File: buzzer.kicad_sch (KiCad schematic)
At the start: 4 parts, among them Q801 2N7002

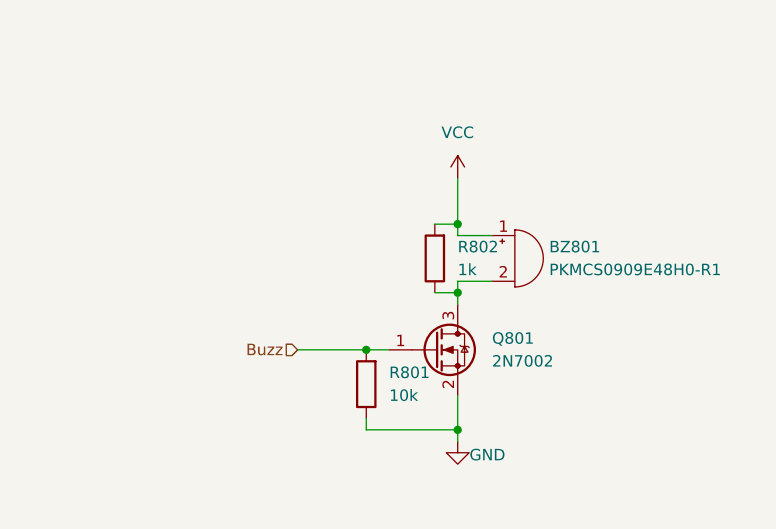
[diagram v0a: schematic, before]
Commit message: Buzzer using high switch
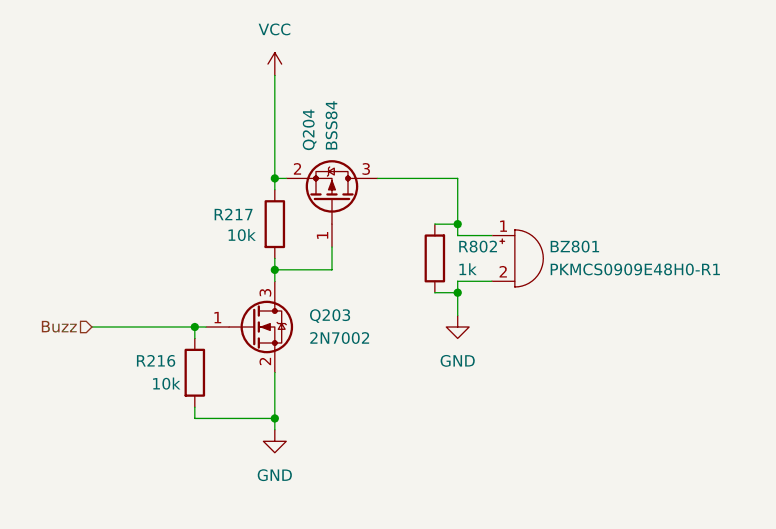
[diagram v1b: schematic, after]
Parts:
- removed Q801: 2N7002, Package_TO_SOT_SMD:SOT-23W_Handsoldering, symbol Transistor_FET:2N7002
- removed R801: 10k, Resistor_SMD:R_1206_3216Metric_Pad1.30x1.75mm_HandSolder, symbol Device:R
- added Q203: 2N7002, Package_TO_SOT_SMD:SOT-23W_Handsoldering, symbol Transistor_FET:2N7002
- added Q204: BSS84, Package_TO_SOT_SMD:SOT-23W_Handsoldering, symbol Transistor_FET:BSS84
- added R216, R217: 10k, Resistor_SMD:R_1206_3216Metric_Pad1.30x1.75mm_HandSolder, symbol Device:R
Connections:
- net Buzz: now also Q203.1 (G), R216.1
- net GND: now also BZ801.2 (-), R802.1, Q203.2 (S), R216.2
- net VCC: now also Q204.2 (S), R217.1; no longer BZ801.1 (+), R802.2
- new net: Q203.3 (D), Q204.1 (G), R217.2
- new net: BZ801.1 (+), Q204.3 (D), R802.2

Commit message: Selected buzzer components
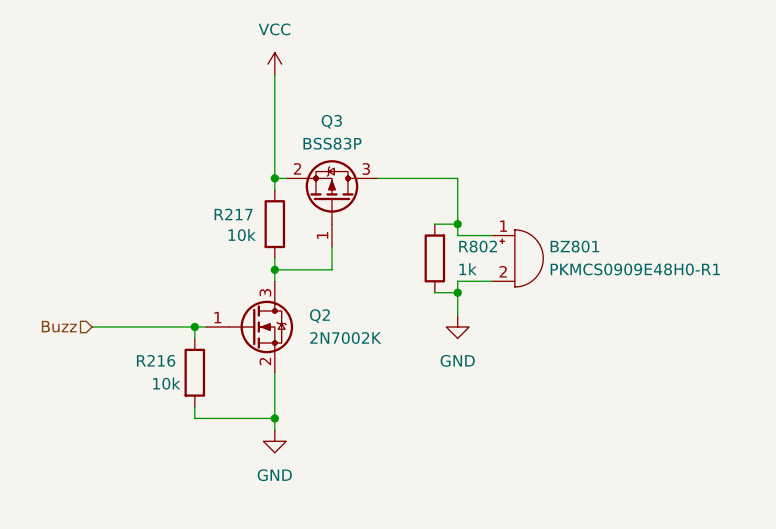
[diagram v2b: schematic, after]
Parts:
- removed Q203: 2N7002, Package_TO_SOT_SMD:SOT-23W_Handsoldering, symbol Transistor_FET:2N7002
- removed Q204: BSS84, Package_TO_SOT_SMD:SOT-23W_Handsoldering, symbol Transistor_FET:BSS84
- added Q2: 2N7002K, Package_TO_SOT_SMD:SOT-23, symbol Transistor_FET:2N7002K
- added Q3: BSS83P, Package_TO_SOT_SMD:SOT-23, symbol Transistor_FET:BSS83P
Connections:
- net Buzz: now also Q2.1 (G)
- net GND: now also Q2.2 (S)
- net VCC: now also Q3.2 (S)
- net at R217.2: now also Q2.3 (D), Q3.1 (G)
- net at BZ801.1 (+), R802.2: now also Q3.3 (D)
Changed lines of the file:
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@@
-	)
-	(symbol
-		(lib_id "Transistor_FET:2N7002")
-		(at 121.92 99.06 0)
-		(unit 1)
-		(exclude_from_sim no)
-		(in_bom yes)
-		(on_board yes)
-		(dnp no)
-		(fields_autoplaced yes)
-		(property "Reference" "Q203"
-			(at 128.27 97.7899 0)
-			(effects
-				(font
-					(size 1.27 1.27)
-				)
-				(justify left)
-			)
-		)
-		(property "Value" "2N7002"
-			(at 128.27 100.3299 0)
-			(effects
-				(font
-					(size 1.27 1.27)
-				)
-				(justify left)
-			)
-		)
-		(property "Footprint" "Package_TO_SOT_SMD:SOT-23W_Handsoldering"
-			(at 127 100.965 0)
-			(effects
-				(font
-					(size 1.27 1.27)
-					(italic yes)
-				)
-				(justify left)
-				(hide yes)
-			)
-		)
-		(property "Datasheet" "https://www.onsemi.com/pub/Collateral/NDS7002A-D.PDF"
-			(at 127 102.87 0)
-			(effects
-				(font
-					(size 1.27 1.27)
-				)
-				(justify left)
-				(hide yes)
-			)
-		)
-		(property "Description" "0.115A Id, 60V Vds, N-Channel MOSFET, SOT-23"
-			(at 121.92 99.06 0)
-			(effects
-				(font
-					(size 1.27 1.27)
-				)
-				(hide yes)
-			)
-		)
-		(pin "3"
-		)
-		(pin "2"
-		)
-		(pin "1"
-		)
-		(instances
-			(project "LifeCounter"
-				(path "/16b3e55a-9d75-49bf-a6fe-25414eb3d7da/ea853267-6be5-4470-9fb8-da1c0cfa6c51"
-					(reference "Q203")
-					(unit 1)
-				)
-			)
-		)
-	)
-	(symbol
-		(lib_id "Transistor_FET:BSS84")
-		(at 130.81 85.09 270)
-		(mirror x)
-		(unit 1)
-		(exclude_from_sim no)
-		(in_bom yes)
-		(on_board yes)
-		(dnp no)
-		(property "Reference" "Q204"
-			(at 128.27 79.502 0)
-			(effects
-				(font
-					(size 1.27 1.27)
-				)
-				(justify left)
-			)
-		)
-		(property "Value" "BSS84"
-			(at 130.81 79.502 0)
-			(effects
-				(font
-					(size 1.27 1.27)
-				)
-				(justify left)
-			)
-		)
-		(property "Footprint" "Package_TO_SOT_SMD:SOT-23W_Handsoldering"
-			(at 128.905 80.01 0)
-			(effects
-				(font
-					(size 1.27 1.27)
-					(italic yes)
-				)
-				(justify left)
-				(hide yes)
-			)
-		)
-		(property "Datasheet" "http://assets.nexperia.com/documents/data-sheet/BSS84.pdf"
-			(at 127 80.01 0)
-			(effects
-				(font
-					(size 1.27 1.27)
-				)
-				(justify left)
-				(hide yes)
-			)
-		)
-		(property "Description" "-0.13A Id, -50V Vds, P-Channel MOSFET, SOT-23"
-			(at 130.81 85.09 0)
-			(effects
-				(font
-					(size 1.27 1.27)
-				)
-				(hide yes)
-			)
-		)
-		(pin "3"
-		)
-		(pin "2"
-		)
-		(pin "1"
-		)
-		(instances
-			(project "LifeCounter"
-				(path "/16b3e55a-9d75-49bf-a6fe-25414eb3d7da/ea853267-6be5-4470-9fb8-da1c0cfa6c51"
-					(reference "Q204")
-					(unit 1)
-				)
-			)
-		)
 	)
 	(symbol
@@
 	)
 	(symbol
+		(lib_id "Transistor_FET:2N7002K")
+		(at 121.92 99.06 0)
+		(unit 1)
+		(exclude_from_sim no)
+		(in_bom yes)
+		(on_board yes)
+		(dnp no)
+		(fields_autoplaced yes)
+		(property "Reference" "Q2"
+			(at 128.27 97.7899 0)
+			(effects
+				(font
+					(size 1.27 1.27)
+				)
+				(justify left)
+			)
+		)
+		(property "Value" "2N7002K"
+			(at 128.27 100.3299 0)
+			(effects
+				(font
+					(size 1.27 1.27)
+				)
+				(justify left)
+			)
+		)
+		(property "Footprint" "Package_TO_SOT_SMD:SOT-23"
+			(at 127 100.965 0)
+			(effects
+				(font
+					(size 1.27 1.27)
+					(italic yes)
+				)
+				(justify left)
+				(hide yes)
+			)
+		)
+		(property "Datasheet" "https://www.diodes.com/assets/Datasheets/ds30896.pdf"
+			(at 127 102.87 0)
+			(effects
+				(font
+					(size 1.27 1.27)
+				)
+				(justify left)
+				(hide yes)
+			)
+		)
+		(property "Description" "0.38A Id, 60V Vds, N-Channel MOSFET, SOT-23"
+			(at 121.92 99.06 0)
+			(effects
+				(font
+					(size 1.27 1.27)
+				)
+				(hide yes)
+			)
+		)
+		(pin "2"
+		)
+		(pin "3"
+		)
+		(pin "1"
+		)
+		(instances
+			(project ""
+				(path "/16b3e55a-9d75-49bf-a6fe-25414eb3d7da/ea853267-6be5-4470-9fb8-da1c0cfa6c51"
+					(reference "Q2")
+					(unit 1)
+				)
+			)
+		)
+	)
+	(symbol
 		(lib_id "Device:R")
 		(at 115.57 104.14 0)
@@
 					(unit 1)
 				)
+			)
+		)
+	)
+	(symbol
+		(lib_id "Transistor_FET:BSS83P")
+		(at 130.81 85.09 270)
+		(mirror x)
+		(unit 1)
+		(exclude_from_sim no)
+		(in_bom yes)
+		(on_board yes)
+		(dnp no)
+		(property "Reference" "Q3"
+			(at 130.81 76.2 90)
+			(effects
+				(font
+					(size 1.27 1.27)
+				)
+			)
+		)
+		(property "Value" "BSS83P"
+			(at 130.81 78.74 90)
+			(effects
+				(font
+					(size 1.27 1.27)
+				)
+			)
+		)
+		(property "Footprint" "Package_TO_SOT_SMD:SOT-23"
+			(at 128.905 80.01 0)
+			(effects
+				(font
+					(size 1.27 1.27)
+					(italic yes)
+				)
+				(justify left)
+				(hide yes)
+			)
+		)
+		(property "Datasheet" "http://www.farnell.com/datasheets/1835997.pdf"
+			(at 127 80.01 0)
+			(effects
+				(font
+					(size 1.27 1.27)
+				)
+				(justify left)
+				(hide yes)
+			)
+		)
+		(property "Description" "-0.33A Id, -60V Vds, P-Channel MOSFET, SOT-23"
+			(at 130.81 85.09 0)
+			(effects
+				(font
+					(size 1.27 1.27)
+				)
+				(hide yes)
+			)
+		)
+		(pin "1"
+		)
+		(pin "3"
+		)
+		(pin "2"
+		)
+		(instances
+			(project ""
+				(path "/16b3e55a-9d75-49bf-a6fe-25414eb3d7da/ea853267-6be5-4470-9fb8-da1c0cfa6c51"
+					(reference "Q3")
+					(unit 1)
+				)

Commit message: Assign component LCSC part numbers
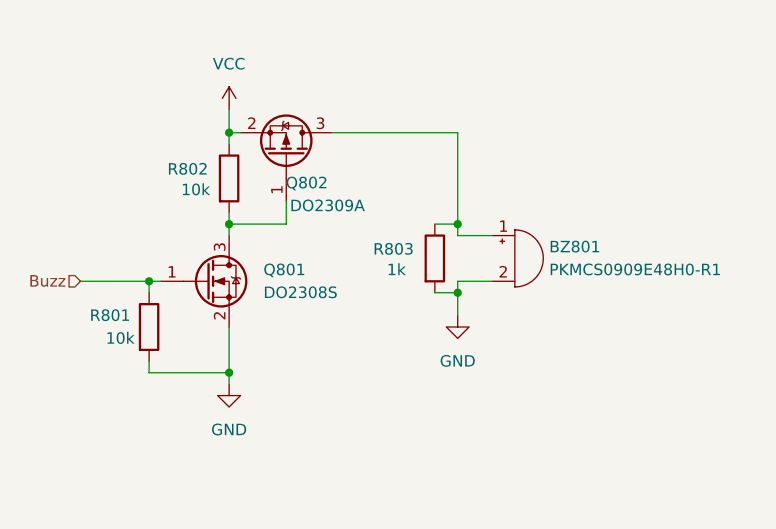
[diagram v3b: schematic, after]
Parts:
- removed Q2: 2N7002K, Package_TO_SOT_SMD:SOT-23, symbol Transistor_FET:2N7002K
- removed Q3: BSS83P, Package_TO_SOT_SMD:SOT-23, symbol Transistor_FET:BSS83P
- removed R216, R217: 10k, Resistor_SMD:R_1206_3216Metric_Pad1.30x1.75mm_HandSolder, symbol Device:R
- added Q801: DO2308S, Package_TO_SOT_SMD:SOT-23_Handsoldering, symbol Transistor_FET:2N7002K
- added Q802: DO2309A, Package_TO_SOT_SMD:SOT-23_Handsoldering, symbol Transistor_FET:BSS83P
- added R801: 10k, Resistor_SMD:R_1206_3216Metric_Pad1.30x1.75mm_HandSolder, symbol Device:R
- added R803: 1k, Resistor_SMD:R_1206_3216Metric_Pad1.30x1.75mm_HandSolder, symbol Device:R
- R802: value 1k -> 10k; now left out of the parts list
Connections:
- net Buzz: now also Q801.1 (G), R801.1
- net GND: now also Q801.2 (S), R801.2, R803.2; no longer R802.1
- net VCC: now also R802.1, Q802.2 (S)
- net at BZ801.1 (+): now also Q802.3 (D), R803.1; no longer R802.2
- new net: Q801.3 (D), Q802.1 (G), R802.2

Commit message: Simplify some schematics to reduce BOM
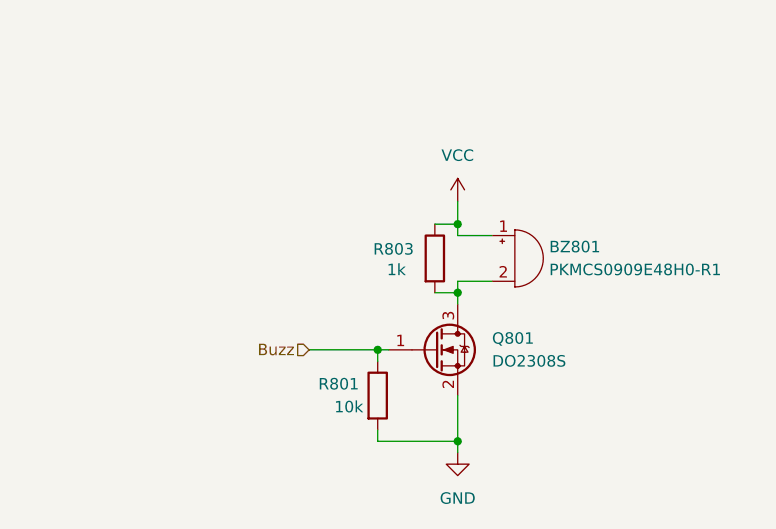
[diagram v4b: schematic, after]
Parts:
- removed Q802: DO2309A, Package_TO_SOT_SMD:SOT-23_Handsoldering, symbol Transistor_FET:BSS83P
- removed R802: 10k, Resistor_SMD:R_1206_3216Metric_Pad1.30x1.75mm_HandSolder, symbol Device:R
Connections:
- net GND: no longer BZ801.2 (-), R803.2
- net VCC: now also BZ801.1 (+), R803.1
- net at Q801.3 (D): now also BZ801.2 (-), R803.2
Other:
- moved on the sheet: Q801, R801

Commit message: Update BOM options for export
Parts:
- BZ801: now left out of the parts list
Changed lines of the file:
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@@
 		(unit 1)
 		(exclude_from_sim no)
-		(in_bom yes)
+		(in_bom no)
 		(on_board yes)
 		(dnp no)
